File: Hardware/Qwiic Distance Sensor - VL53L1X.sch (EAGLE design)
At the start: 27 parts, among them J2 SMD, J3 PTH, J4 SMD, U2 VL53L1X

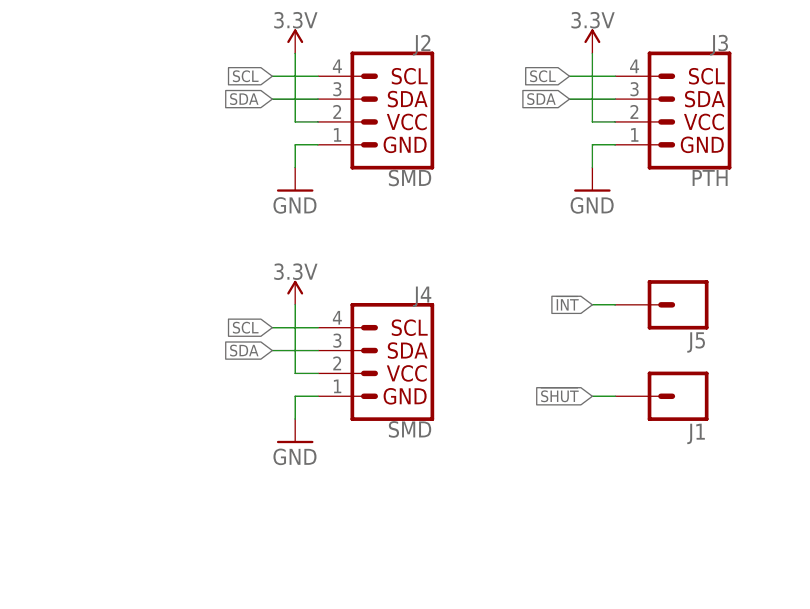
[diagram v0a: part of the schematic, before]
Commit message: updating Qwiic connectors
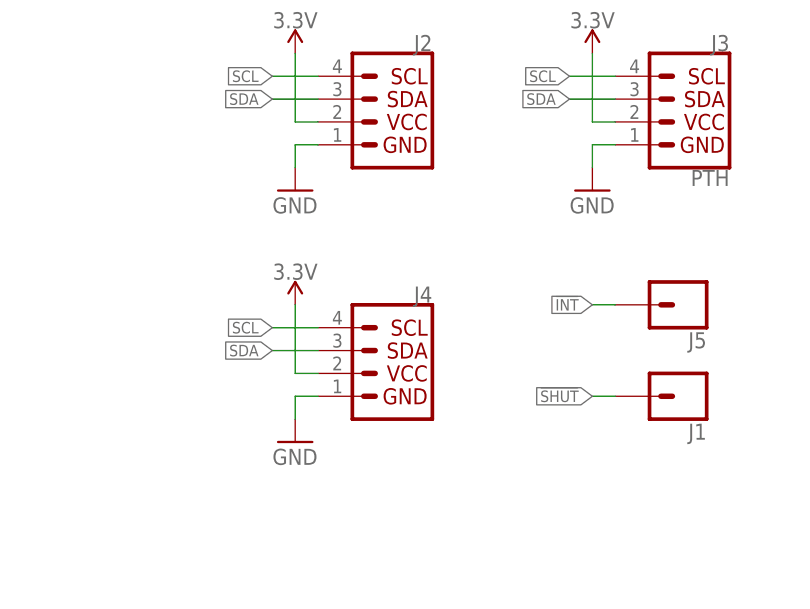
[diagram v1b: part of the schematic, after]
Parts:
- J2, J4: value SMD -> (none); device SparkX:I2C_STANDARDJS-1MM -> SparkFun-Connectors:QWIIC_CONNECTORJS-1MM
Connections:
- net 3.3V: now also J2.2, J4.2; no longer J2.VCC, J4.VCC
- net GND: now also J2.1, J4.1; no longer J2.GND, J4.GND
- net SCL: now also J2.4, J4.4; no longer J2.SCL, J4.SCL
- net SDA: now also J2.3, J4.3; no longer J2.SDA, J4.SDA
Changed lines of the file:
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@@
 <layer number="59" name="tCarbon" color="7" fill="1" visible="no" active="no"/>
 <layer number="60" name="bCarbon" color="7" fill="1" visible="no" active="no"/>
+<layer number="88" name="SimResults" color="9" fill="1" visible="no" active="yes"/>
+<layer number="89" name="SimProbes" color="9" fill="1" visible="no" active="yes"/>
 <layer number="90" name="Modules" color="5" fill="1" visible="no" active="no"/>
 <layer number="91" name="Nets" color="2" fill="1" visible="yes" active="yes"/>
@@
 <part name="SUPPLY5" library="SparkFun-PowerSymbols" deviceset="3.3V" device=""/>
 <part name="GND4" library="SparkFun" deviceset="GND" device=""/>
-<part name="J2" library="SparkX" deviceset="I2C_STANDARD" device="JS-1MM" value="SMD"/>
+<part name="J2" library="SparkFun-Connectors" deviceset="QWIIC_CONNECTOR" device="JS-1MM"/>
 <part name="GND6" library="SparkFun" deviceset="GND" device=""/>
 <part name="SUPPLY7" library="SparkFun-PowerSymbols" deviceset="3.3V" device=""/>
@@
 <part name="C4" library="SparkFun-Capacitors" deviceset="0.1UF" device="-0603-25V-(+80/-20%)" value="0.1uF"/>
 <part name="SUPPLY8" library="SparkFun-PowerSymbols" deviceset="3.3V" device=""/>
-<part name="J4" library="SparkX" deviceset="I2C_STANDARD" device="JS-1MM" value="SMD"/>
+<part name="J4" library="SparkFun-Connectors" deviceset="QWIIC_CONNECTOR" device="JS-1MM"/>
 <part name="GND8" library="SparkFun" deviceset="GND" device=""/>
 <part name="LOGO1" library="SparkFun-Aesthetics" deviceset="OSHW-LOGO" device="MINI"/>
@@
 </segment>
 <segment>
-<pinref part="J2" gate="G$1" pin="VCC"/>
+<pinref part="J2" gate="G$1" pin="2"/>
 <wire x1="53.34" y1="58.42" x2="50.8" y2="58.42" width="0.1524" layer="91"/>
 <wire x1="50.8" y1="58.42" x2="50.8" y2="66.04" width="0.1524" layer="91"/>
@@
 </segment>
 <segment>
-<pinref part="J4" gate="G$1" pin="VCC"/>
+<pinref part="J4" gate="G$1" pin="2"/>
 <wire x1="53.34" y1="30.48" x2="50.8" y2="30.48" width="0.1524" layer="91"/>
 <wire x1="50.8" y1="30.48" x2="50.8" y2="38.1" width="0.1524" layer="91"/>
@@
 </segment>
 <segment>
-<pinref part="J2" gate="G$1" pin="GND"/>
+<pinref part="J2" gate="G$1" pin="1"/>
 <wire x1="53.34" y1="55.88" x2="50.8" y2="55.88" width="0.1524" layer="91"/>
 <wire x1="50.8" y1="55.88" x2="50.8" y2="53.34" width="0.1524" layer="91"/>
@@
 </segment>
 <segment>
-<pinref part="J4" gate="G$1" pin="GND"/>
+<pinref part="J4" gate="G$1" pin="1"/>
 <wire x1="53.34" y1="27.94" x2="50.8" y2="27.94" width="0.1524" layer="91"/>
 <wire x1="50.8" y1="27.94" x2="50.8" y2="25.4" width="0.1524" layer="91"/>
@@
 <net name="SCL" class="0">
 <segment>
-<pinref part="J2" gate="G$1" pin="SCL"/>
+<pinref part="J2" gate="G$1" pin="4"/>
 <wire x1="53.34" y1="63.5" x2="48.26" y2="63.5" width="0.1524" layer="91"/>
 <label x="48.26" y="63.5" size="1.27" layer="95" font="vector" rot="R180" xref="yes"/>
@@
 </segment>
 <segment>
-<pinref part="J4" gate="G$1" pin="SCL"/>
+<pinref part="J4" gate="G$1" pin="4"/>
 <wire x1="53.34" y1="35.56" x2="48.26" y2="35.56" width="0.1524" layer="91"/>
 <label x="48.26" y="35.56" size="1.27" layer="95" font="vector" rot="R180" xref="yes"/>
@@
 <net name="SDA" class="0">
 <segment>
-<pinref part="J2" gate="G$1" pin="SDA"/>
+<pinref part="J2" gate="G$1" pin="3"/>
 <wire x1="53.34" y1="60.96" x2="48.26" y2="60.96" width="0.1524" layer="91"/>
 <label x="48.26" y="60.96" size="1.27" layer="95" font="vector" rot="R180" xref="yes"/>
@@
 </segment>
 <segment>
-<pinref part="J4" gate="G$1" pin="SDA"/>
+<pinref part="J4" gate="G$1" pin="3"/>
 <wire x1="53.34" y1="33.02" x2="48.26" y2="33.02" width="0.1524" layer="91"/>
 <label x="48.26" y="33.02" size="1.27" layer="95" font="vector" rot="R180" xref="yes"/>

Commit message: post review changes
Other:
- note added: "VCC: 2.3V-3.5V"
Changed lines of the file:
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@@
 <text x="62.23" y="77.47" size="1.27" layer="97" font="vector">2</text>
 <text x="101.6" y="177.8" size="1.778" layer="97" font="vector">VL53L1X Distance Sensor</text>
+<text x="101.6" y="175.26" size="1.778" layer="97">VCC: 2.3V-3.5V</text>
 </plain>
 <instances>

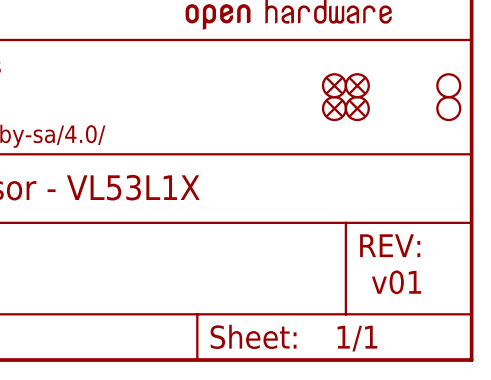
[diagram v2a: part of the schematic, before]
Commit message: Fixing issues
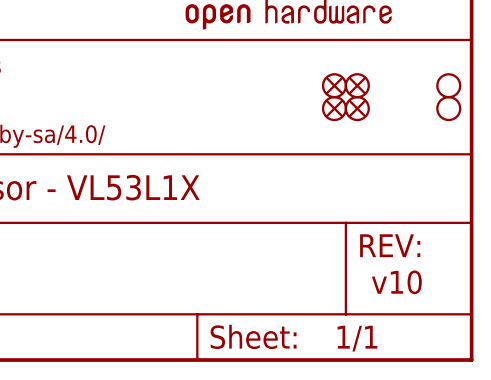
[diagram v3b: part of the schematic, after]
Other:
- note added: "v10"
- note removed: "v01"
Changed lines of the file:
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@@
 <?xml version="1.0" encoding="utf-8"?>
 <!DOCTYPE eagle SYSTEM "eagle.dtd">
-<eagle version="7.7.0">
+<eagle version="9.0.1">
 <drawing>
 <settings>
-<setting alwaysvectorfont="yes"/>
+<setting alwaysvectorfont="no"/>
+<setting keepoldvectorfont="yes"/>
 <setting verticaltext="up"/>
 </settings>
@@
 <sheet>
 <plain>
-<text x="170.434" y="11.43" size="2.54" layer="94">N. Seidle</text>
-<text x="237.744" y="7.366" size="2.54" layer="94" font="vector">v01</text>
+<text x="170.434" y="11.43" size="2.54" layer="94" font="vector">N. Seidle</text>
+<text x="237.744" y="7.366" size="2.54" layer="94" font="vector">v10</text>
 <text x="91.44" y="109.22" size="1.778" layer="97" font="vector">7-bit unshifted I2C address: 0x29</text>
 <text x="157.48" y="149.86" size="1.778" layer="97" font="vector">Clear Jumper to remove
